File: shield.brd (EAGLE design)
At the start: 36.2 x 26.7 mm, 12 parts

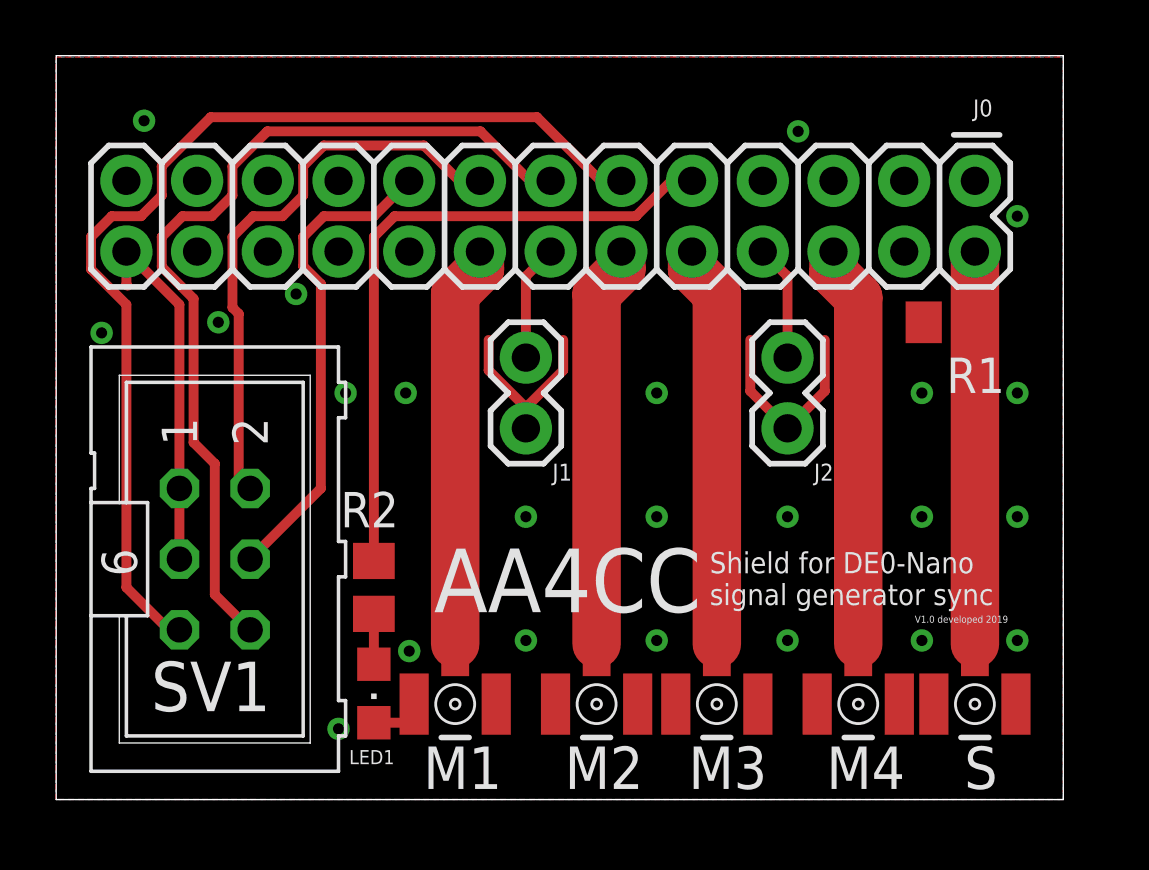
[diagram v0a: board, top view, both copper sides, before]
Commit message: Getting rid of weird airwave between R1 and pin 2 of J0
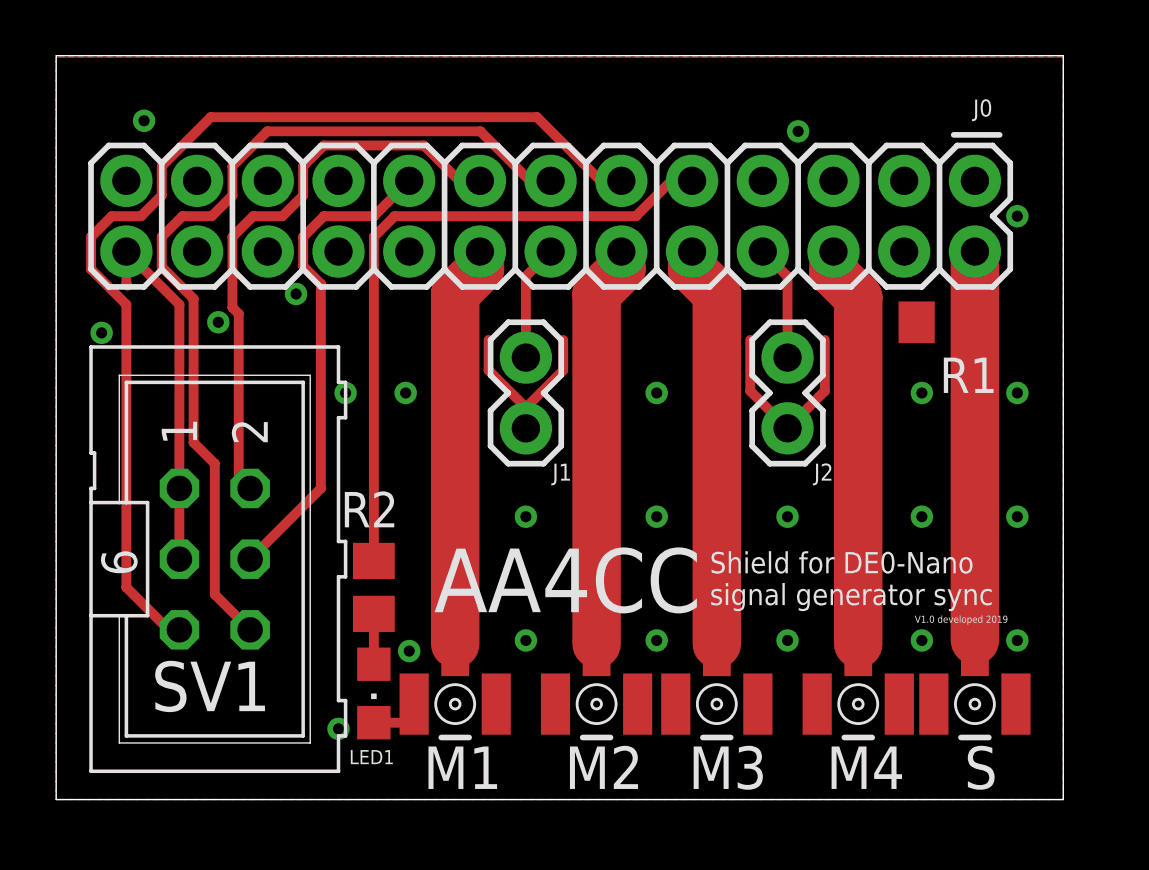
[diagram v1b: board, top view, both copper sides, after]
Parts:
- moved R1 0.25 mm to (43.9, 28.6)
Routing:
- net N$1: track 14.7 -> 17.3 mm
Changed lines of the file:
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@@
 <attribute name="VALUE" x="26.035" y="18.415" size="1.27" layer="27" rot="R90"/>
 </element>
-<element name="R1" library="rcl" library_urn="urn:adsk.eagle:library:334" package="R0805" package3d_urn="urn:adsk.eagle:package:23553/2" value="200" x="44.196" y="28.575" smashed="yes">
-<attribute name="NAME" x="44.069" y="26.035" size="1.27" layer="25"/>
-<attribute name="POPULARITY" value="86" x="64.516" y="8.255" size="1.778" layer="27" display="off"/>
-<attribute name="SPICEPREFIX" value="R" x="64.516" y="8.255" size="1.778" layer="27" display="off"/>
+<element name="R1" library="rcl" library_urn="urn:adsk.eagle:library:334" package="R0805" package3d_urn="urn:adsk.eagle:package:23553/2" value="200" x="43.942" y="28.575" smashed="yes">
+<attribute name="NAME" x="43.815" y="26.035" size="1.27" layer="25"/>
+<attribute name="POPULARITY" value="86" x="64.262" y="8.255" size="1.778" layer="27" display="off"/>
+<attribute name="SPICEPREFIX" value="R" x="64.262" y="8.255" size="1.778" layer="27" display="off"/>
 </element>
 <element name="X_M1" library="con-coax" library_urn="urn:adsk.eagle:library:133" package="MC-921" package3d_urn="urn:adsk.eagle:package:6223/1" value="MC-921" x="40.894" y="14.859" smashed="yes">
@@
 <contactref element="R1" pad="2"/>
 <contactref element="J0" pad="2"/>
-<wire x1="45.085" y1="16.3865" x2="45.085" y2="17.018" width="0.254" layer="1"/>
-<wire x1="45.085" y1="17.018" x2="45.085" y2="31.115" width="1.74193125" layer="1"/>
-<wire x1="45.085" y1="31.115" x2="45.146" y2="28.575" width="0" layer="19" extent="1-1"/>
+<wire x1="45.085" y1="17.145" x2="45.085" y2="16.3865" width="0.254" layer="1"/>
+<wire x1="45.085" y1="31.115" x2="45.085" y2="17.145" width="1.74193125" layer="1"/>
+<wire x1="44.892" y1="28.575" x2="45.085" y2="28.768" width="0.254" layer="1"/>
+<wire x1="45.085" y1="28.768" x2="45.085" y2="31.115" width="0.254" layer="1"/>
 </signal>
 <signal name="N$19">
